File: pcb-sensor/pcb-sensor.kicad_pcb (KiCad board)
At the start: 2 copper layers, 86 x 86 mm, 28 parts, among them J1 Conn_02x06_Counter_Clockwise, J2 Conn_01x03, J3 Conn_01x01, J4 Conn_01x05, J5 Conn_01x02, J6 Conn_01x03, J7 Conn_01x01, J8 Conn_01x01, U1 LM340MP, U2 SFH617A-1, U4 SFH617A-1

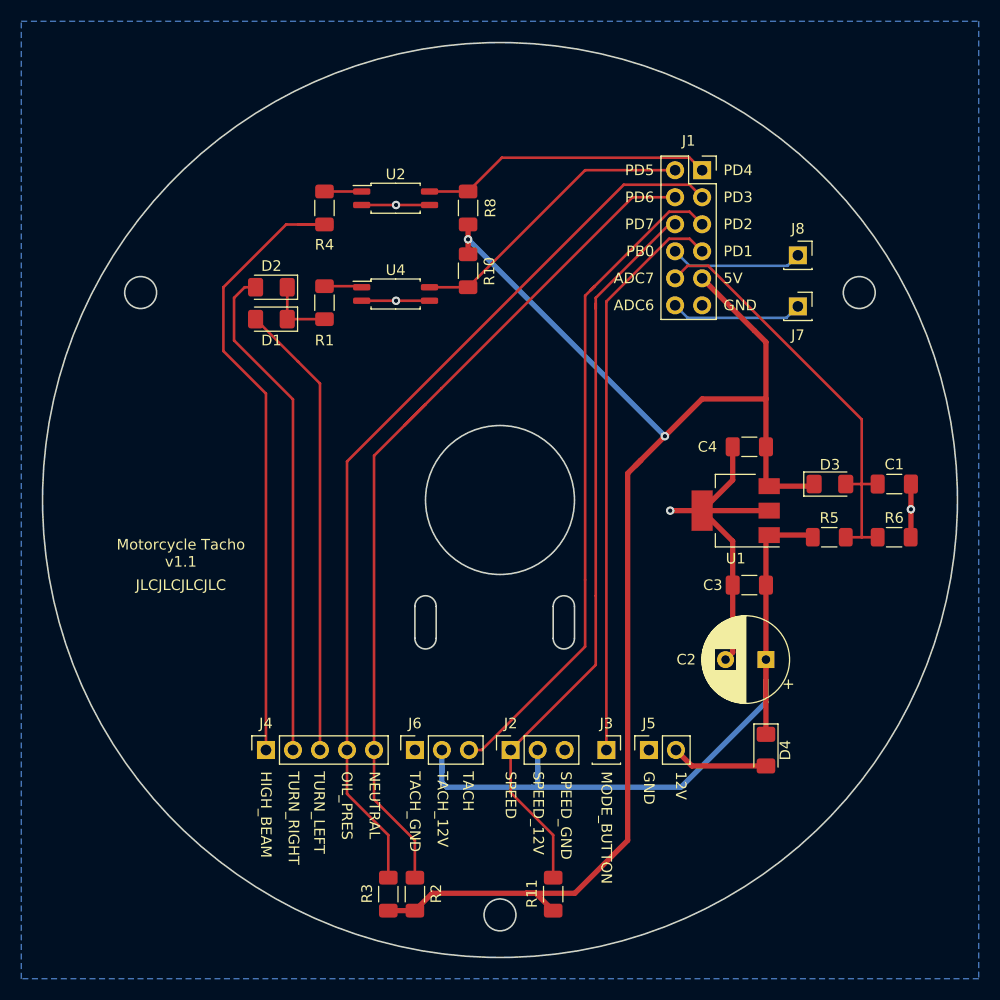
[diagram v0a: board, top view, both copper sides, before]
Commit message: resolves #37: optocoupler footprint
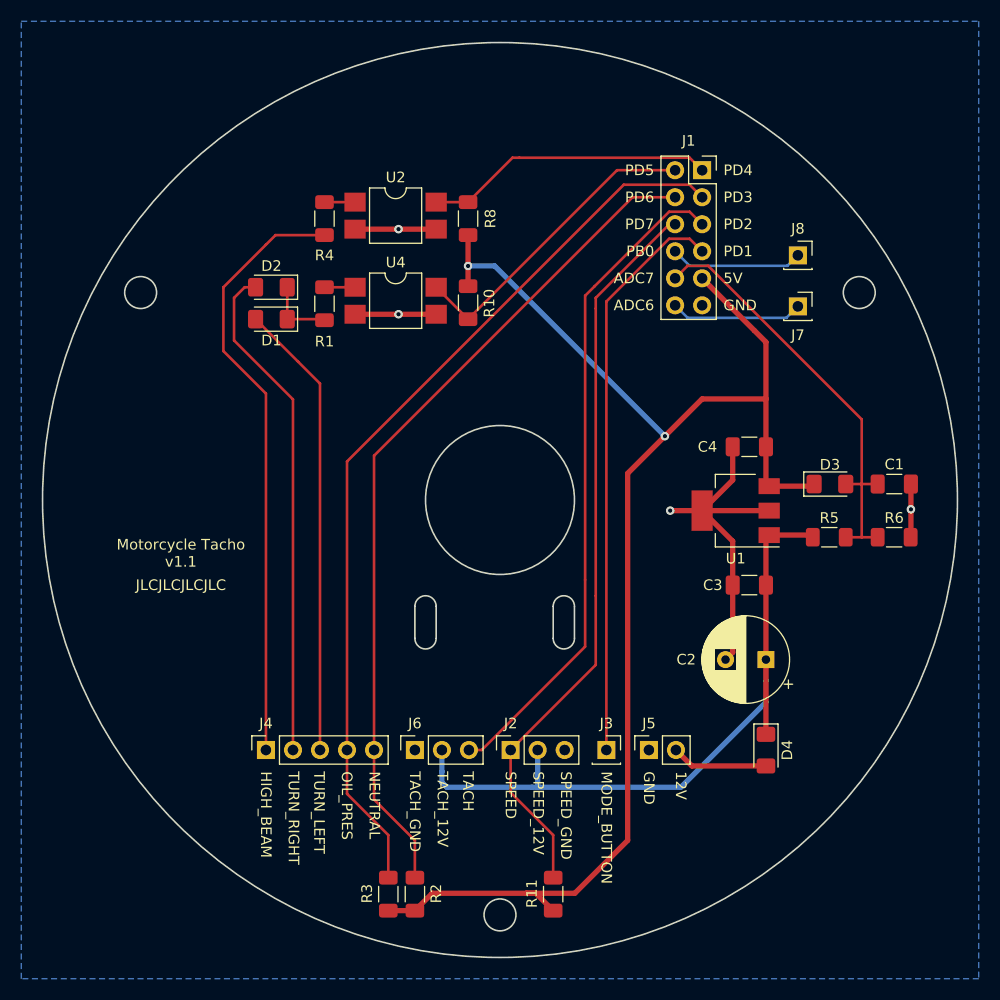
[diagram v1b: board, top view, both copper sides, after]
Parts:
- U2, U4: value SFH617A-1 -> SFH617A-2X009T; footprint Package_SO:SOP-4_4.4x2.6mm_P1.27mm -> Package_DIP:SMDIP-4_W7.62mm
- moved R10 3.00 mm to (147.0, 81.5)
- moved U2 1.63 mm to (140.2, 73.3)
- moved R4 1.00 mm to (133.5, 73.5)
- moved R8 1.00 mm to (147.0, 73.5)
- moved U4 0.64 mm to (140.2, 81.3)
- moved R1 0.10 mm to (133.5, 81.5)
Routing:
- net +12V: track 71.0 -> 67.6 mm
- net /HIGH_BEAM: track 59.6 -> 56.7 mm
- net /NEUTRAL: track 82.4 -> 79.6 mm
- net GND: track 49.7 -> 52.2 mm
- net /PD5: track 27.6 -> 29.5 mm
- net Net-(R1-Pad2): track 3.54 -> 2.88 mm
- net Net-(R4-Pad2): track 3.50 -> 2.88 mm
- net /PD2: track 63.3 -> 62.7 mm
